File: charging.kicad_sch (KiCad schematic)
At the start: 17 parts, among them Q1 2N7002, SW1 SW_SPDT, U2 BQ24075RGT

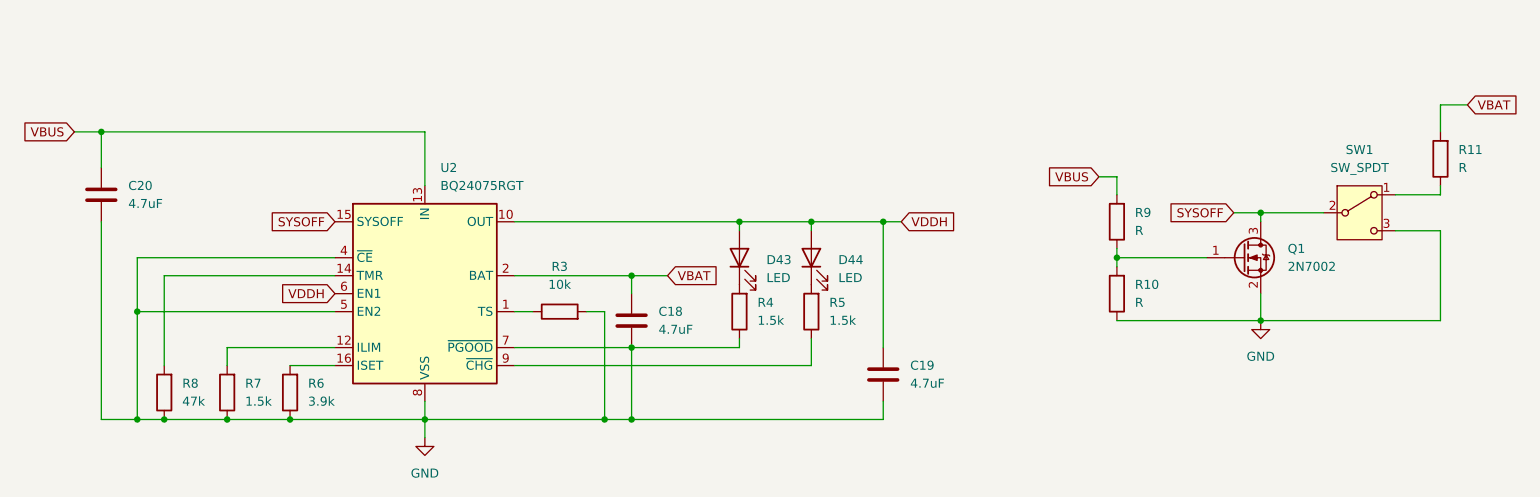
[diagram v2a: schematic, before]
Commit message: Route CPU and charging circuit
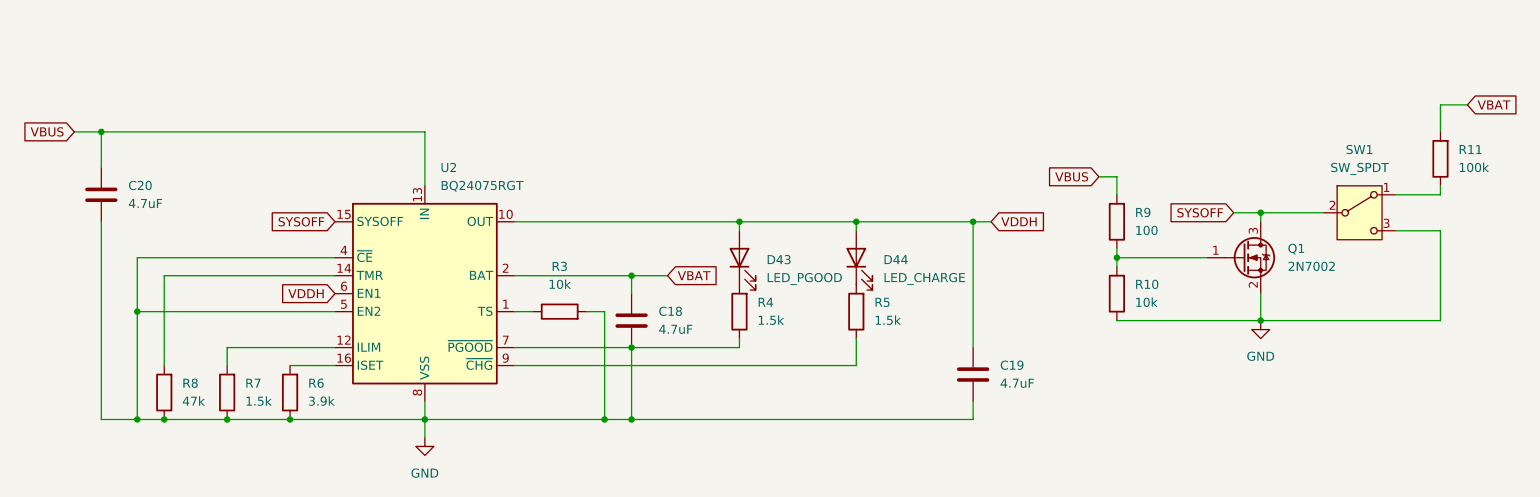
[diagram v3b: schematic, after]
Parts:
- C18, C19, C20: footprint (none) -> Capacitor_SMD:C_0603_1608Metric
- D43: value LED -> LED_PGOOD; footprint (none) -> LED_SMD:LED_0603_1608Metric
- D44: value LED -> LED_CHARGE; footprint (none) -> LED_SMD:LED_0603_1608Metric
- R10: value R -> 10k; footprint (none) -> Resistor_SMD:R_0603_1608Metric
- R11: value R -> 100k; footprint (none) -> Resistor_SMD:R_0603_1608Metric
- R3, R4, R5, R6, R7, R8: footprint (none) -> Resistor_SMD:R_0603_1608Metric
- R9: value R -> 100; footprint (none) -> Resistor_SMD:R_0603_1608Metric
- SW1: footprint (none) -> Button_Switch_SMD:SW_SPDT_PCM12
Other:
- moved on the sheet: C19, D44, R5
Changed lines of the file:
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@@
   (junction (at 102.87 88.9) (diameter 0) (color 0 0 0 0)
   )
-  (junction (at 138.43 71.12) (diameter 0) (color 0 0 0 0)
+  (junction (at 151.13 71.12) (diameter 0) (color 0 0 0 0)
   )
   (junction (at 99.06 99.06) (diameter 0) (color 0 0 0 0)
@@
   (junction (at 36.83 99.06) (diameter 0) (color 0 0 0 0)
   )
-  (junction (at 128.27 71.12) (diameter 0) (color 0 0 0 0)
+  (junction (at 134.62 71.12) (diameter 0) (color 0 0 0 0)
   )
   (junction (at 33.02 99.06) (diameter 0) (color 0 0 0 0)
@@
     (stroke (width 0) (type default))
   )
-  (wire (pts (xy 86.36 91.44) (xy 128.27 91.44))
+  (wire (pts (xy 86.36 91.44) (xy 134.62 91.44))
     (stroke (width 0) (type default))
   )
@@
     (stroke (width 0) (type default))
   )
-  (wire (pts (xy 138.43 71.12) (xy 138.43 88.9))
+  (wire (pts (xy 151.13 71.12) (xy 151.13 88.9))
     (stroke (width 0) (type default))
   )
@@
     (stroke (width 0) (type default))
   )
-  (wire (pts (xy 128.27 71.12) (xy 128.27 72.39))
+  (wire (pts (xy 134.62 71.12) (xy 134.62 72.39))
     (stroke (width 0) (type default))
   )
@@
     (stroke (width 0) (type default))
   )
-  (wire (pts (xy 128.27 91.44) (xy 128.27 87.63))
+  (wire (pts (xy 134.62 91.44) (xy 134.62 87.63))
     (stroke (width 0) (type default))
   )
@@
     (stroke (width 0) (type default))
   )
-  (wire (pts (xy 138.43 99.06) (xy 138.43 96.52))
+  (wire (pts (xy 151.13 99.06) (xy 151.13 96.52))
     (stroke (width 0) (type default))
   )
@@
     (stroke (width 0) (type default))
   )
-  (wire (pts (xy 102.87 99.06) (xy 138.43 99.06))
+  (wire (pts (xy 102.87 99.06) (xy 151.13 99.06))
     (stroke (width 0) (type default))
   )
@@
     (stroke (width 0) (type default))
   )
-  (wire (pts (xy 128.27 71.12) (xy 118.11 71.12))
+  (wire (pts (xy 134.62 71.12) (xy 118.11 71.12))
     (stroke (width 0) (type default))
   )
@@
     (stroke (width 0) (type default))
   )
-  (wire (pts (xy 138.43 71.12) (xy 128.27 71.12))
+  (wire (pts (xy 151.13 71.12) (xy 134.62 71.12))
     (stroke (width 0) (type default))
   )
@@
     (stroke (width 0) (type default))
   )
-  (wire (pts (xy 140.97 71.12) (xy 138.43 71.12))
+  (wire (pts (xy 153.67 71.12) (xy 151.13 71.12))
     (stroke (width 0) (type default))
   )
@@
     )
   )
-  (global_label "VDDH" (shape input) (at 140.97 71.12 0) (fields_autoplaced)
+  (global_label "VDDH" (shape input) (at 153.67 71.12 0) (fields_autoplaced)
     (effects (font (size 1.27 1.27)) (justify left))
-    (property "Intersheetrefs" "${INTERSHEET_REFS}" (at 148.9143 71.12 0)
+    (property "Intersheetrefs" "${INTERSHEET_REFS}" (at 161.6143 71.12 0)
       (effects (font (size 1.27 1.27)) (justify left) hide)
     )
@@
       (effects (font (size 1.27 1.27)) (justify right))
     )
-    (property "Footprint" "" (at 56.388 95.25 90)
+    (property "Footprint" "Resistor_SMD:R_0603_1608Metric" (at 56.388 95.25 90)
       (effects (font (size 1.27 1.27)) hide)
     )
@@
       (effects (font (size 1.27 1.27)) (justify right))
     )
-    (property "Footprint" "" (at 38.608 95.25 90)
+    (property "Footprint" "Resistor_SMD:R_0603_1608Metric" (at 38.608 95.25 90)
       (effects (font (size 1.27 1.27)) hide)
     )
@@
       (effects (font (size 1.27 1.27)) (justify right))
     )
-    (property "Footprint" "" (at 47.498 95.25 90)
+    (property "Footprint" "Resistor_SMD:R_0603_1608Metric" (at 47.498 95.25 90)
       (effects (font (size 1.27 1.27)) hide)
     )
@@
     )
   )
-  (symbol (lib_id "Device:LED") (at 128.27 76.2 90) (unit 1)
-    (in_bom yes) (on_board yes) (dnp no) (fields_autoplaced)
-    (property "Reference" "D44" (at 132.08 76.5175 90)
-      (effects (font (size 1.27 1.27)) (justify right))
-    )
-    (property "Value" "LED" (at 132.08 79.0575 90)
-      (effects (font (size 1.27 1.27)) (justify right))
-    )
-    (property "Footprint" "" (at 128.27 76.2 0)
-      (effects (font (size 1.27 1.27)) hide)
-    )
-    (property "Datasheet" "~" (at 128.27 76.2 0)
+  (symbol (lib_id "Device:LED") (at 134.62 76.2 90) (unit 1)
+    (in_bom yes) (on_board yes) (dnp no) (fields_autoplaced)
+    (property "Reference" "D44" (at 138.43 76.5175 90)
+      (effects (font (size 1.27 1.27)) (justify right))
+    )
+    (property "Value" "LED_CHARGE" (at 138.43 79.0575 90)
+      (effects (font (size 1.27 1.27)) (justify right))
+    )
+    (property "Footprint" "LED_SMD:LED_0603_1608Metric" (at 134.62 76.2 0)
+      (effects (font (size 1.27 1.27)) hide)
+    )
+    (property "Datasheet" "~" (at 134.62 76.2 0)
       (effects (font (size 1.27 1.27)) hide)
     )
@@
       (effects (font (size 1.27 1.27)) (justify right))
     )
-    (property "Value" "R" (at 173.99 72.39 0)
-      (effects (font (size 1.27 1.27)) (justify right))
-    )
-    (property "Footprint" "" (at 173.228 71.12 90)
+    (property "Value" "100" (at 173.99 72.39 0)
+      (effects (font (size 1.27 1.27)) (justify right))
+    )
+    (property "Footprint" "Resistor_SMD:R_0603_1608Metric" (at 173.228 71.12 90)
       (effects (font (size 1.27 1.27)) hide)
     )
@@
       (effects (font (size 1.27 1.27)))
     )
-    (property "Footprint" "" (at 205.74 69.85 0)
+    (property "Footprint" "Button_Switch_SMD:SW_SPDT_PCM12" (at 205.74 69.85 0)
       (effects (font (size 1.27 1.27)) hide)
     )
@@
       (effects (font (size 1.27 1.27)) (justify right))
     )
-    (property "Value" "R" (at 219.71 63.5 0)
-      (effects (font (size 1.27 1.27)) (justify right))
-    )
-    (property "Footprint" "" (at 218.948 62.23 90)
+    (property "Value" "100k" (at 219.71 63.5 0)
+      (effects (font (size 1.27 1.27)) (justify right))
+    )
+    (property "Footprint" "Resistor_SMD:R_0603_1608Metric" (at 218.948 62.23 90)
       (effects (font (size 1.27 1.27)) hide)
     )
@@
       (effects (font (size 1.27 1.27)))
     )
-    (property "Footprint" "" (at 92.71 85.598 90)
+    (property "Footprint" "Resistor_SMD:R_0603_1608Metric" (at 92.71 85.598 90)
       (effects (font (size 1.27 1.27)) hide)
     )
@@
       (effects (font (size 1.27 1.27)) (justify left))
     )
-    (property "Footprint" "" (at 28.9052 71.12 0)
+    (property "Footprint" "Capacitor_SMD:C_0603_1608Metric" (at 28.9052 71.12 0)
       (effects (font (size 1.27 1.27)) hide)
     )
@@
       (effects (font (size 1.27 1.27)) (justify right))
     )
-    (property "Value" "R" (at 173.99 82.55 0)
-      (effects (font (size 1.27 1.27)) (justify right))
-    )
-    (property "Footprint" "" (at 173.228 81.28 90)
+    (property "Value" "10k" (at 173.99 82.55 0)
+      (effects (font (size 1.27 1.27)) (justify right))
+    )
+    (property "Footprint" "Resistor_SMD:R_0603_1608Metric" (at 173.228 81.28 90)
       (effects (font (size 1.27 1.27)) hide)
     )
@@
       (effects (font (size 1.27 1.27)) (justify right))
     )
-    (property "Value" "LED" (at 121.92 79.0575 90)
-      (effects (font (size 1.27 1.27)) (justify right))
-    )
-    (property "Footprint" "" (at 118.11 76.2 0)
+    (property "Value" "LED_PGOOD" (at 121.92 79.0575 90)
+      (effects (font (size 1.27 1.27)) (justify right))
+    )
+    (property "Footprint" "LED_SMD:LED_0603_1608Metric" (at 118.11 76.2 0)
       (effects (font (size 1.27 1.27)) hide)
     )
@@
       (effects (font (size 1.27 1.27)) (justify right))
     )
-    (property "Footprint" "" (at 119.888 83.82 90)
+    (property "Footprint" "Resistor_SMD:R_0603_1608Metric" (at 119.888 83.82 90)
       (effects (font (size 1.27 1.27)) hide)
     )
@@
       (effects (font (size 1.27 1.27)) (justify left))
     )
-    (property "Footprint" "" (at 103.8352 88.9 0)
+    (property "Footprint" "Capacitor_SMD:C_0603_1608Metric" (at 103.8352 88.9 0)
       (effects (font (size 1.27 1.27)) hide)
     )
@@
     )
   )
-  (symbol (lib_id "Device:R") (at 128.27 83.82 180) (unit 1)
-    (in_bom yes) (on_board yes) (dnp no) (fields_autoplaced)
-    (property "Reference" "R5" (at 130.81 82.55 0)
-      (effects (font (size 1.27 1.27)) (justify right))
-    )
-    (property "Value" "1.5k" (at 130.81 85.09 0)
-      (effects (font (size 1.27 1.27)) (justify right))
-    )
-    (property "Footprint" "" (at 130.048 83.82 90)
-      (effects (font (size 1.27 1.27)) hide)
-    )
-    (property "Datasheet" "~" (at 128.27 83.82 0)
+  (symbol (lib_id "Device:R") (at 134.62 83.82 180) (unit 1)
+    (in_bom yes) (on_board yes) (dnp no) (fields_autoplaced)
+    (property "Reference" "R5" (at 137.16 82.55 0)
+      (effects (font (size 1.27 1.27)) (justify right))
+    )
+    (property "Value" "1.5k" (at 137.16 85.09 0)
+      (effects (font (size 1.27 1.27)) (justify right))
+    )
+    (property "Footprint" "Resistor_SMD:R_0603_1608Metric" (at 136.398 83.82 90)
+      (effects (font (size 1.27 1.27)) hide)
+    )
+    (property "Datasheet" "~" (at 134.62 83.82 0)
       (effects (font (size 1.27 1.27)) hide)
     )
@@
     )
   )
-  (symbol (lib_id "Device:C") (at 138.43 92.71 0) (unit 1)
-    (in_bom yes) (on_board yes) (dnp no) (fields_autoplaced)
-    (property "Reference" "C19" (at 142.24 91.44 0)
-      (effects (font (size 1.27 1.27)) (justify left))
-    )
-    (property "Value" "4.7uF" (at 142.24 93.98 0)
-      (effects (font (size 1.27 1.27)) (justify left))
-    )
-    (property "Footprint" "" (at 139.3952 96.52 0)
-      (effects (font (size 1.27 1.27)) hide)
-    )
-    (property "Datasheet" "~" (at 138.43 92.71 0)
-      (effects (font (size 1.27 1.27)) hide)
-    )
+  (symbol (lib_id "Device:C") (at 151.13 92.71 0) (unit 1)
+    (in_bom yes) (on_board yes) (dnp no) (fields_autoplaced)
+    (property "Reference" "C19" (at 154.94 91.44 0)
+      (effects (font (size 1.27 1.27)) (justify left))
+    )
+    (property "Value" "4.7uF" (at 154.94 93.98 0)
+      (effects (font (size 1.27 1.27)) (justify left))
+    )
+    (property "Footprint" "Capacitor_SMD:C_0603_1608Metric" (at 152.0952 96.52 0)
+      (effects (font (size 1.27 1.27)) hide)
+    )
+    (property "Datasheet" "~" (at 151.13 92.71 0)
+      (effects (font (size 1.27 1.27)) hide)
+    )

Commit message: first jlc submission
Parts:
- SW1: LCSC (none) -> C431541
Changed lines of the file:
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@@
+      (effects (font (size 1.27 1.27)) hide)
+    )
+    (property "LCSC" "C431541" (at 205.74 69.85 0)
       (effects (font (size 1.27 1.27)) hide)
     )
